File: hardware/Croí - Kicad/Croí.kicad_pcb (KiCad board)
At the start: 2 copper layers, 100 x 100 mm, 40 parts, among them J1 Conn_ARM_JTAG_SWD_10, J2 2060-1452/998-404, J3 ESQ-110-14-G-D, J4 Conn_02x03_Odd_Even, J5 USB_C_Receptacle_USB2.0_16P, U1 W25Q128JVS, U2 TPS563203, U3 STM32F072C8Tx, U4 BME680, U5 BMP390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

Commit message: started pcb work
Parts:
- moved C23 163.6 mm to (229.0, 135.0)
- moved C19 121.7 mm to (202.0, 37.5)
- moved C21 120.5 mm to (233.0, 135.0)
- moved D1 118.5 mm to (229.0, 131.5)
- moved U7 117.7 mm to (234.0, 132.0)
- moved C24 107.0 mm to (47.5, 137.5)
- moved C25 107.0 mm to (47.5, 139.5)
- moved C22 105.3 mm to (51.0, 141.5)
- moved C26 101.6 mm to (62.0, 138.0)
- moved R6 101.2 mm to (59.0, 137.0)
- moved R7 99.8 mm to (59.0, 138.5)
- moved D2 99.5 mm to (59.5, 133.0), turned to 90 degrees
- moved U8 94.0 mm to (53.4, 137.6)
- moved U4 92.6 mm to (200.8, 34.2)
- moved C5 82.9 mm to (162.0, 24.0)
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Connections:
- U1 pad 6: SWCLK -> SPICLK
- U3 pad 15: unconnected-(U3-PA5-Pad15) -> SPICLK
- U4 pad 4: SWCLK -> SPICLK
- U5 pad 2: SWCLK -> SPICLK

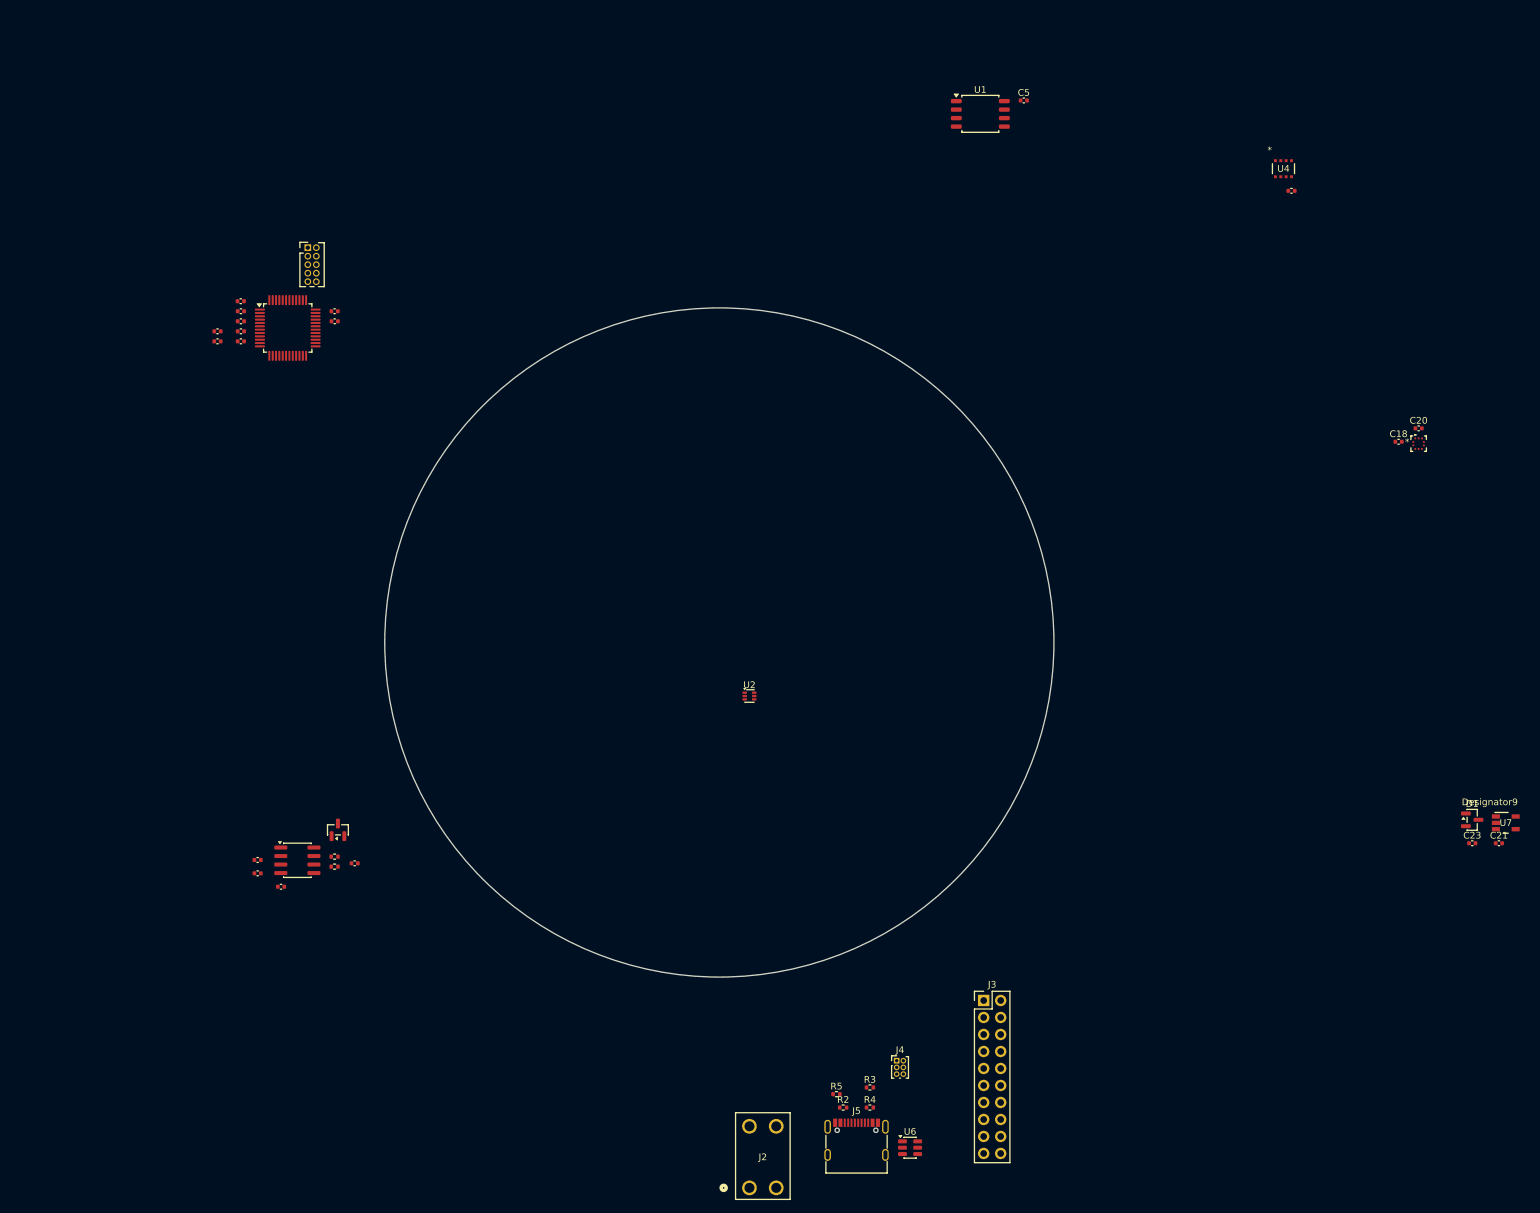
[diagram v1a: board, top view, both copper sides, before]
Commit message: Finalised board with accelerometer and IMU
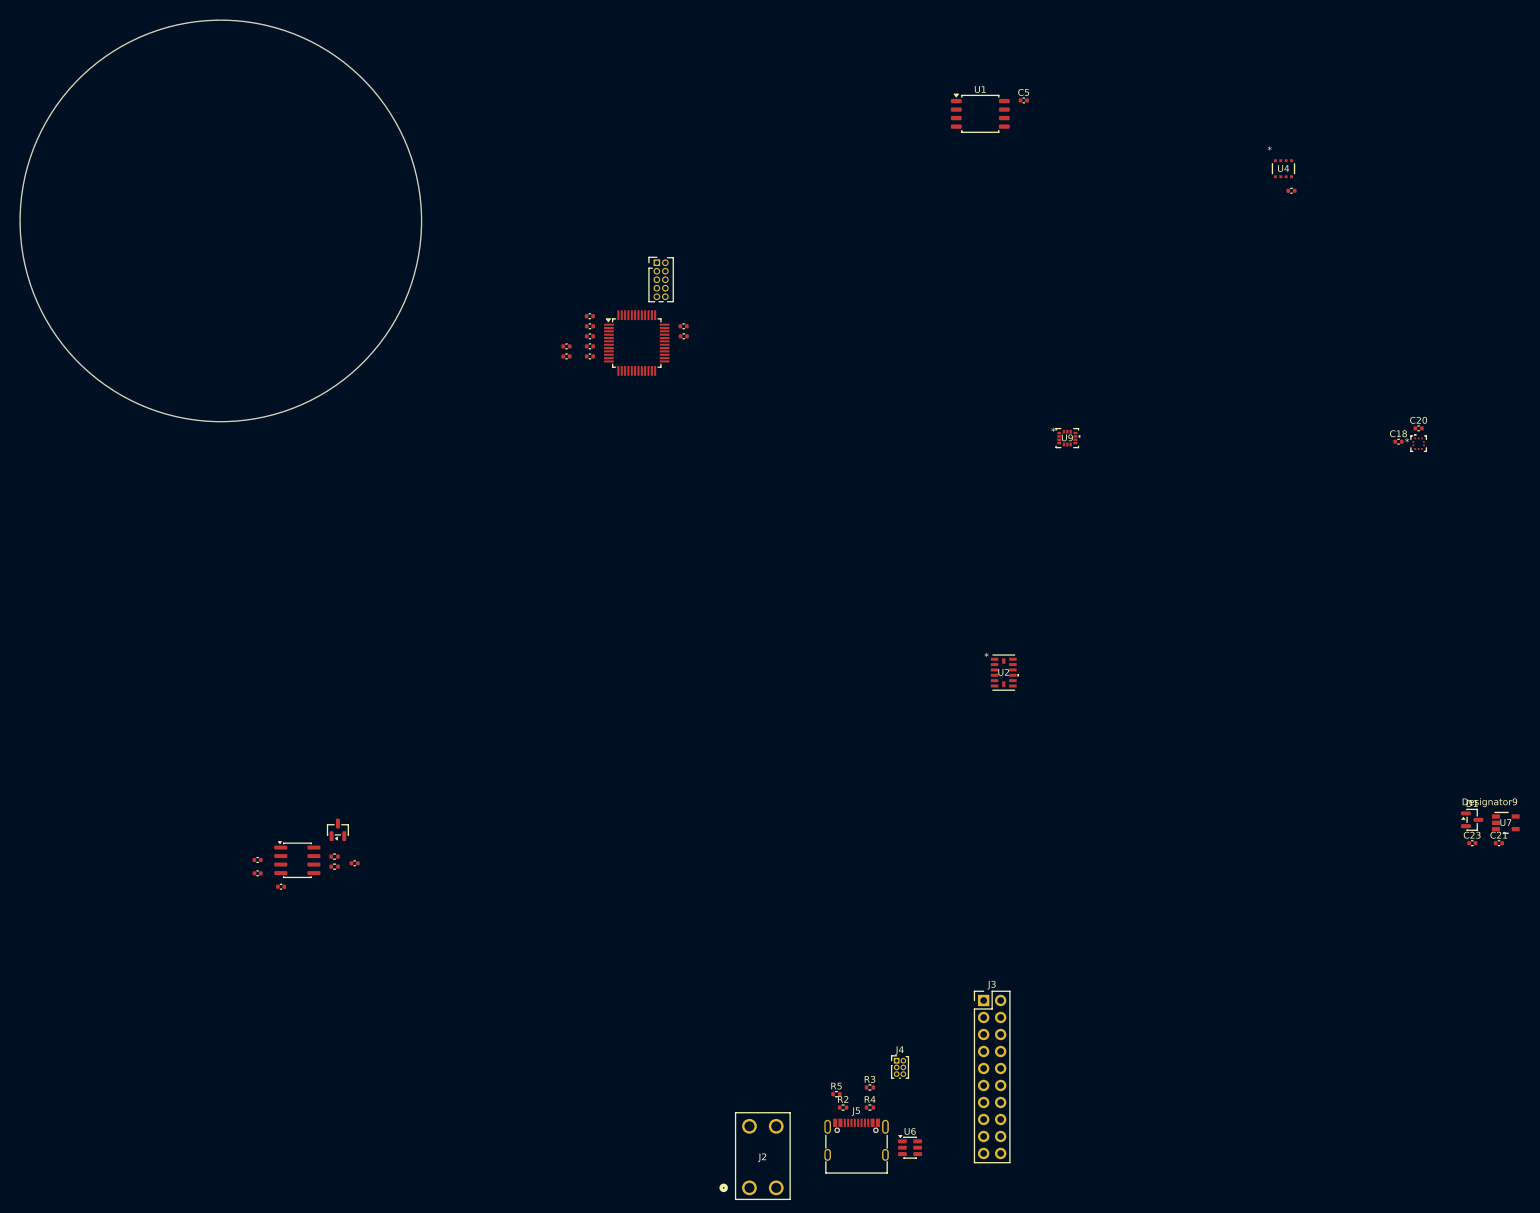
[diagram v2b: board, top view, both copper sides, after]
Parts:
- added U9: LSM6DSO32TR, footprints:LGA-14L_2P5X3X0P83_STM, F.Cu at (168.5, 74.5)
- U2: value TPS563203 -> ADXL375BCCZ; footprint Package_TO_SOT_SMD:SOT-563 -> footprints:LGA_CC-14-1_ADI
- moved C17 52.2 mm to (111.2, 59.2)
- moved C2 52.2 mm to (97.1, 56.2)
- moved C10 52.2 mm to (93.7, 60.8)
- moved C12 52.2 mm to (93.7, 62.2)
- moved C15 52.2 mm to (111.2, 57.8)
- moved C4 52.2 mm to (97.2, 57.8)
- moved C6 52.2 mm to (97.2, 59.2)
- moved C7 52.2 mm to (97.2, 60.8)
- moved C8 52.2 mm to (97.2, 62.2)
- moved J1 52.2 mm to (107.2, 48.2)
- moved U3 52.2 mm to (104.2, 60.2)
- moved U2 38.2 mm to (159.0, 109.5)
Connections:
- U2 pad 1: VBAT -> 3.3V
- U2 pad 2: Net-(U2-SW) -> GND
- U2 pad 3: GND -> unconnected-(U2-RESERVED-Pad3)
- U2 pad 4: Net-(U2-BST) -> GND
- U2 pad 5: Net-(U2-EN) -> GND
- U2 pad 6: Net-(U2-FB) -> 3.3V
- U3 pad 22: unconnected-(U3-PB11-Pad22) -> IMU_CS
- U3 pad 28: unconnected-(U3-PB15-Pad28) -> ACCELEROMETER_CS
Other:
- board size 100 x 100 mm -> 60 x 60 mm

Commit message: summaries are hard
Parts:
- removed J1: Conn_ARM_JTAG_SWD_10, Connector_PinHeader_1.27mm:PinHeader_2x05_P1.27mm_Vertical
- added C1: 100nF, Capacitor_SMD:C_0402_1005Metric, F.Cu at (52.5, 39.5)
- added C11: 1uF, Capacitor_SMD:C_0402_1005Metric, F.Cu at (44.0, 38.5)
- added C3: 1uF, Capacitor_SMD:C_0402_1005Metric, F.Cu at (52.5, 42.5)
- added C9: 100nF, Capacitor_SMD:C_0402_1005Metric, F.Cu at (44.0, 37.5)
- added J6: Conn_02x03_Odd_Even, Connector_PinHeader_1.00mm:PinHeader_2x03_P1.00mm_Vertical, F.Cu at (44.5, 49.0)
- added Q1: IPP060N06N, Package_TO_SOT_THT:TO-220-3_Vertical, F.Cu at (50.5, 18.0)
- J3: footprint Connector_PinHeader_2.54mm:PinHeader_2x10_P2.54mm_Vertical -> footprints:SAMTEC_ESQ-110-14-G-D
- J4: moved to B.Cu
- moved C21 208.1 mm to (52.5, 31.5)
- moved U7 206.2 mm to (52.0, 35.0), turned to -90 degrees
- moved C23 206.0 mm to (49.5, 34.0), turned to 90 degrees
- moved D1 205.2 mm to (51.5, 28.5), turned to -90 degrees
- moved C18 196.0 mm to (25.5, 38.2), turned to 180 degrees
- moved C20 196.0 mm to (28.5, 36.2)
- moved U5 196.0 mm to (28.5, 38.5)
- moved J2 181.7 mm to (40.0, 23.8)
- moved U4 166.9 mm to (34.0, 38.5), turned to 90 degrees
- moved C19 165.5 mm to (36.5, 38.5), turned to -90 degrees
- moved U6 158.8 mm to (42.0, 59.6), turned to -90 degrees
- moved R2 153.6 mm to (38.5, 55.0), turned to -90 degrees
- moved R5 152.4 mm to (37.0, 55.0), turned to 90 degrees
- moved J4 152.0 mm to (43.0, 53.0), turned to -90 degrees
- moved R4 150.5 mm to (39.0, 62.0), turned to 180 degrees
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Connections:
- J2 pad 1: VBAT -> Net-(J2-1_1)
- J2 pad 2: VBAT -> Net-(J2-1_1)
- J3 pad 10: 5VSERVO -> unconnected-(J3-Pad10)
- J3 pad 11: 5VSERVO -> unconnected-(J3-Pad11)
- J3 pad 12: 5VSERVO -> unconnected-(J3-Pad12)
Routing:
- net 3.3V: track 0.00 -> 67.3 mm, vias 0 -> 3
- net VBUS_RAW: track 0.00 -> 58.0 mm, vias 0 -> 3
- net SPICLK: track 0.00 -> 57.4 mm, vias 0 -> 3
- net SPI_MISO: track 0.00 -> 48.2 mm, vias 0 -> 5
- net SPI_MOSI: track 0.00 -> 46.7 mm, vias 0 -> 4
- net GND: track 0.00 -> 26.4 mm
- net ACCELEROMETER_CS: track 0.00 -> 25.9 mm, vias 0 -> 2
- net BMP390_CS: track 0.00 -> 24.7 mm, vias 0 -> 2
- net Flash_CS: track 0.00 -> 20.7 mm, vias 0 -> 2
- net Net-(J2-1_1): track 0.00 -> 19.8 mm
- net IMU_CS: track 0.00 -> 15.4 mm, vias 0 -> 2
- net NRST: track 0.00 -> 15.2 mm, vias 0 -> 2
- net BME680_CS: track 0.00 -> 14.8 mm, vias 0 -> 2
- net 5VLOGIC: track 0.00 -> 7.56 mm
- net Net-(J5-D+-PadA6): track 0.00 -> 6.83 mm
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- added copper zone on B.Cu, net GND
- added copper zone on F.Cu, net GND
- added copper zone on In1.Cu, net GND
- added copper zone on In2.Cu, net GND
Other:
- outline, holes or cut-outs redrawn
- copper layers 2 -> 4
- board text added: "*"

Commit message: changed some stuff
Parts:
- removed D1: BAT54C, Package_TO_SOT_SMD:SOT-23
- removed J4: Conn_02x03_Odd_Even, Connector_PinHeader_1.00mm:PinHeader_2x03_P1.00mm_Vertical
- removed J5: USB_C_Receptacle_USB2.0_16P, Connector_USB:USB_C_Receptacle_G-Switch_GT-USB-7010ASV
- removed R2, R5: 10K, Resistor_SMD:R_0402_1005Metric
- removed R3, R4: 5.1K, Resistor_SMD:R_0402_1005Metric
- removed U6: USBLC6-2SC6, Package_TO_SOT_SMD:SOT-23-6
- moved C7 17.7 mm to (35.7, 40.8), turned to 0 degrees
- moved C8 8.29 mm to (31.0, 49.0)
- moved C5 8.23 mm to (28.5, 41.1), turned to 180 degrees
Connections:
- C21 pad 1: Net-(U7-IN) -> VBAT
- U3 pad 32: PA- -> CAN-
- U3 pad 33: PA+ -> CAN+
- U7 pad 2: Net-(U7-IN) -> VBAT
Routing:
- net VBUS_RAW: track 58.0 -> 0.00 mm, vias 3 -> 0
- net 3.3V: track 67.3 -> 87.6 mm, vias 3 -> 4
- net GND: track 26.4 -> 40.8 mm, vias 0 -> 11
- net Net-(J5-D+-PadA6): track 6.83 -> 0.00 mm
- net Net-(J5-D--PadA7): track 6.66 -> 0.00 mm
- net VBAT: track 4.52 -> 11.1 mm
- net Net-(U7-IN): track 4.29 -> 0.00 mm
- net Net-(J5-CC1): track 2.79 -> 0.00 mm
- net Net-(J5-CC2): track 2.58 -> 0.00 mm

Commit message: crazy work
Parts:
- removed J6: Conn_02x03_Odd_Even, Connector_PinHeader_1.00mm:PinHeader_2x03_P1.00mm_Vertical
- added J1: JTAG-10 PIN, Connector_IDC:IDC-Header_2x05_P2.54mm_Vertical, F.Cu at (36.9, 67.0)
- J2: value 2060-1452/998-404 -> XT30PW-M; footprint footprints:WAG -> footprints:AMASS_XT30PW-M
- moved C4 22.1 mm to (39.0, 40.5), turned to 180 degrees
- moved C6 18.5 mm to (40.0, 52.5), turned to 180 degrees
- moved C2 11.1 mm to (30.0, 49.0)
- moved J2 10.0 mm to (42.0, 14.0)
- moved Q1 4.74 mm to (52.0, 22.5)
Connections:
- J3 pad 01: GND -> unconnected-(J3-Pad01)
- J3 pad 02: GND -> unconnected-(J3-Pad02)
- J3 pad 03: 5VLOGIC -> GND
- J3 pad 04: 5VLOGIC -> GND
- J3 pad 10: unconnected-(J3-Pad10) -> NRST
- J3 pad 13: GND -> unconnected-(J3-Pad13)
- J3 pad 15: CAN_out- -> SWDIO
- J3 pad 17: GND -> SWCLK
- J3 pad 18: GND -> CAN_out-
- Q1 pad 2: Net-(J2-1_1) -> Net-(Q1-D)
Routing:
- net 3.3V: track 87.6 -> 160.3 mm, vias 4 -> 7
- net NRST: track 15.2 -> 59.5 mm, vias 2 -> 1
- net 5VLOGIC: track 7.56 -> 32.9 mm
- net CAN-: track 0.00 -> 24.5 mm, vias 0 -> 2
- net CAN+: track 0.00 -> 23.9 mm, vias 0 -> 2
- net GND: track 40.8 -> 62.9 mm, vias 11 -> 15
- net Net-(J2-1_1): track 19.8 -> 0.00 mm
- net SWCLK: track 2.86 -> 18.7 mm, vias 0 -> 1
- net Net-(Q1-D): track 0.00 -> 13.4 mm
- net SWDIO: track 6.20 -> 14.1 mm
- net CAN_out+: track 4.58 -> 12.3 mm
- net CAN_out-: track 4.58 -> 11.6 mm
- net VBAT: track 11.1 -> 6.01 mm

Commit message: Board Routing completed: Ready for Review
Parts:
- moved C26 34.4 mm to (59.0, 43.0), turned to 180 degrees
- moved R6 31.2 mm to (58.5, 45.0), turned to 90 degrees
- moved R7 30.7 mm to (58.5, 50.0), turned to 90 degrees
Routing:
- net Net-(C26-Pad1): track 0.00 -> 11.4 mm, vias 0 -> 2
- net GND: track 62.9 -> 65.4 mm
- net CAN_out+: track 12.3 -> 13.9 mm
- net CAN_out-: track 11.6 -> 13.1 mm

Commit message: minor changes
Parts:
- added C13: 100nF, Capacitor_SMD:C_0402_1005Metric, F.Cu at (34.4, 53.2)
- added C27: 8pF, Capacitor_SMD:C_0402_1005Metric, F.Cu at (33.0, 47.7)
- added C28: 8pF, Capacitor_SMD:C_0402_1005Metric, F.Cu at (33.0, 52.7)
- added G***: LOGO, LOGO, F.Cu at (53.0, 37.0)
- added R1: 10KΩ, Resistor_SMD:R_0402_1005Metric, F.Cu at (41.0, 45.0)
- added XTAL1: NX3225GD-8MHZ-STD-CRA-3, footprints2:XTAL_NX3225GD-8MHZ-STD-CRA-3_NDK, F.Cu at (33.8, 50.2)
- R6, R7: value 60 Ω -> 60Ω
- moved Q1 19.4 mm to (33.0, 18.7)
- moved U7 18.6 mm to (34.0, 30.2)
- moved C21 18.5 mm to (34.5, 27.1)
- moved C7 18.5 mm to (43.8, 57.4), turned to 180 degrees
- moved C23 18.5 mm to (31.4, 30.2)
- moved C18 18.0 mm to (43.2, 34.8)
- moved C12 17.7 mm to (35.7, 53.3)
- moved C10 17.3 mm to (35.5, 54.8), turned to 0 degrees
- moved C20 17.0 mm to (45.5, 36.5), turned to -90 degrees
- moved U5 15.1 mm to (43.5, 36.7), turned to -90 degrees
- moved C8 14.8 mm to (43.8, 56.4), turned to 180 degrees
- moved C3 11.1 mm to (41.5, 43.9), turned to 0 degrees
- moved C1 9.27 mm to (44.3, 43.9), turned to 180 degrees
- moved C6 7.57 mm to (39.0, 45.0), turned to 0 degrees
- moved U9 7.28 mm to (37.5, 35.8)
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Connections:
- J1 pad 2: SWCLK -> SWCLK2
- J3 pad 10: NRST -> SWCLK2
- J3 pad 17: SWCLK -> NRST
- U3 pad 26: Mode_sel -> unconnected-(U3-PB13-Pad26)
- U3 pad 37: SWCLK -> SWCLK2
- U3 pad 44: unconnected-(U3-BOOT0-Pad44) -> Net-(U3-BOOT0)
- U3 pad 5: unconnected-(U3-PF0-Pad5) -> Net-(U3-PF0)
- U3 pad 6: unconnected-(U3-PF1-Pad6) -> Net-(U3-PF1)
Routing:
- net SWCLK2: track 0.00 -> 48.4 mm, vias 0 -> 2
- net SWDIO: track 14.1 -> 55.3 mm, vias 0 -> 2
- net GND: track 65.4 -> 30.4 mm, vias 15 -> 36
- net IMU_CS: track 15.4 -> 46.3 mm
- net CAN-: track 24.5 -> 5.71 mm, vias 2 -> 0
- net SWCLK: track 18.7 -> 0.00 mm, vias 1 -> 0
- net CAN+: track 23.9 -> 5.71 mm, vias 2 -> 0
- net SPI_MISO: track 48.2 -> 36.6 mm, vias 5 -> 3
- net Net-(C26-Pad1): track 11.4 -> 0.00 mm, vias 2 -> 0
- net BMP390_CS: track 24.7 -> 13.4 mm
- net ACCELEROMETER_CS: track 25.9 -> 15.2 mm
- net 3.3V: track 160.3 -> 150.0 mm, vias 7 -> 11
- net SPICLK: track 57.4 -> 47.4 mm, vias 3 -> 5
- net Flash_CS: track 20.7 -> 27.4 mm
- net Net-(Q1-D): track 13.4 -> 7.66 mm
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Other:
- board text added: "Croi v1.0"

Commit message: Memes added, Dervla might recognise someone
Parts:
- added G***: LOGO, LOGO, F.Cu at (53.0, 35.5)
- added G***: LOGO, LOGO, B.Cu at (43.0, 41.5)
- moved G*** 34.2 mm to (19.5, 44.0)
